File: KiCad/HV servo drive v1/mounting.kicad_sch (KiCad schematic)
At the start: 11 parts

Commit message: KiCad 8.0 update
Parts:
- renumbered H14 to H1, H8 to H10, H3 to H11, H13 to H2, H12 to H3, H10 to H4, H9 to H5, H4 to H8, H1 to H9

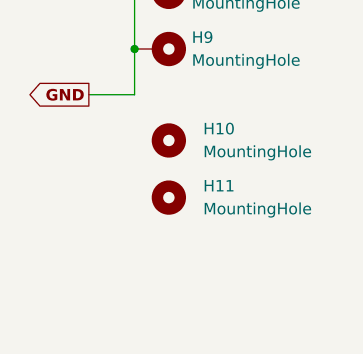
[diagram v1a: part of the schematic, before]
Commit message: start rev 2 changes
fix component references, fix rj45 and dc-dc converter footprints, add RLC filters on all power connectors, add more mounting holes
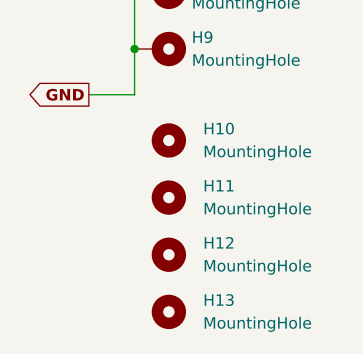
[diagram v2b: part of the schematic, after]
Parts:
- added H12, H13: MountingHole, footprints:MountingHole_3.2mm_M3_Pad_TopBottom_LargeIsolation, symbol Mechanical:MountingHole
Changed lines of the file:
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@@
+	)
+	(symbol
+		(lib_id "Mechanical:MountingHole")
+		(at 143.51 128.27 270)
+		(unit 1)
+		(exclude_from_sim no)
+		(in_bom yes)
+		(on_board yes)
+		(dnp no)
+		(fields_autoplaced yes)
+		(property "Reference" "H12"
+			(at 147.32 127 90)
+			(effects
+				(font
+					(size 1.27 1.27)
+				)
+				(justify left)
+			)
+		)
+		(property "Value" "MountingHole"
+			(at 147.32 129.54 90)
+			(effects
+				(font
+					(size 1.27 1.27)
+				)
+				(justify left)
+			)
+		)
+		(property "Footprint" "footprints:MountingHole_3.2mm_M3_Pad_TopBottom_LargeIsolation"
+			(at 143.51 128.27 0)
+			(effects
+				(font
+					(size 1.27 1.27)
+				)
+				(hide yes)
+			)
+		)
+		(property "Datasheet" "~"
+			(at 143.51 128.27 0)
+			(effects
+				(font
+					(size 1.27 1.27)
+				)
+				(hide yes)
+			)
+		)
+		(property "Description" ""
+			(at 143.51 128.27 0)
+			(effects
+				(font
+					(size 1.27 1.27)
+				)
+				(hide yes)
+			)
+		)
+		(instances
+			(project "HV servo drive v1"
+				(path "/00e1489f-e855-42b2-9b8a-dcc958a4feb6/5630d7aa-18e9-4c19-993b-fb61da4e222f"
+					(reference "H12")
+					(unit 1)
+				)
+			)
+		)
 	)
 	(symbol
@@
 					(unit 1)
 				)
+			)
+		)
+	)
+	(symbol
+		(lib_id "Mechanical:MountingHole")
+		(at 143.51 134.62 270)
+		(unit 1)
+		(exclude_from_sim no)
+		(in_bom yes)
+		(on_board yes)
+		(dnp no)
+		(fields_autoplaced yes)
+		(property "Reference" "H13"
+			(at 147.32 133.35 90)
+			(effects
+				(font
+					(size 1.27 1.27)
+				)
+				(justify left)
+			)
+		)
+		(property "Value" "MountingHole"
+			(at 147.32 135.89 90)
+			(effects
+				(font
+					(size 1.27 1.27)
+				)
+				(justify left)
+			)
+		)
+		(property "Footprint" "footprints:MountingHole_3.2mm_M3_Pad_TopBottom_LargeIsolation"
+			(at 143.51 134.62 0)
+			(effects
+				(font
+					(size 1.27 1.27)
+				)
+				(hide yes)
+			)
+		)
+		(property "Datasheet" "~"
+			(at 143.51 134.62 0)
+			(effects
+				(font
+					(size 1.27 1.27)
+				)
+				(hide yes)
+			)
+		)
+		(property "Description" ""
+			(at 143.51 134.62 0)
+			(effects
+				(font
+					(size 1.27 1.27)
+				)
+				(hide yes)
+			)
+		)
+		(instances
+			(project "HV servo drive v1"
+				(path "/00e1489f-e855-42b2-9b8a-dcc958a4feb6/5630d7aa-18e9-4c19-993b-fb61da4e222f"
+					(reference "H13")
+					(unit 1)
+				)

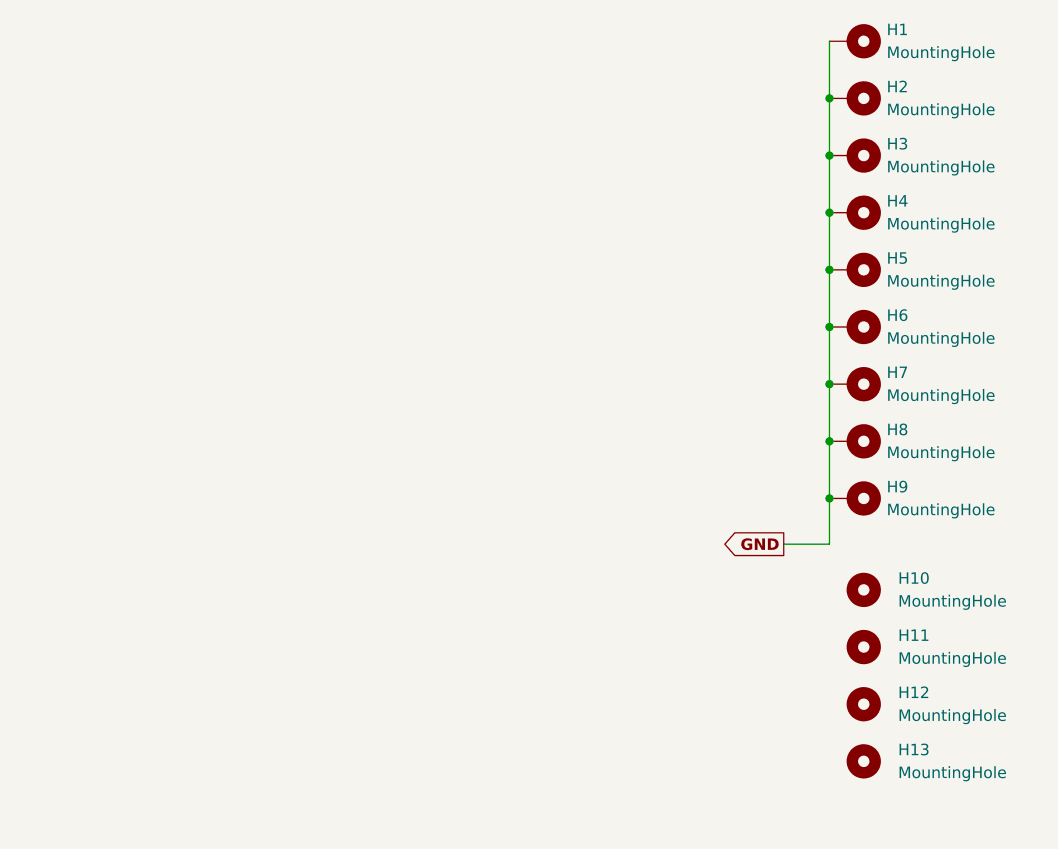
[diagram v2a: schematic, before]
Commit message: update to rev 2.1
basically the same version as in the FOC youtube video, with some minor issues fixed
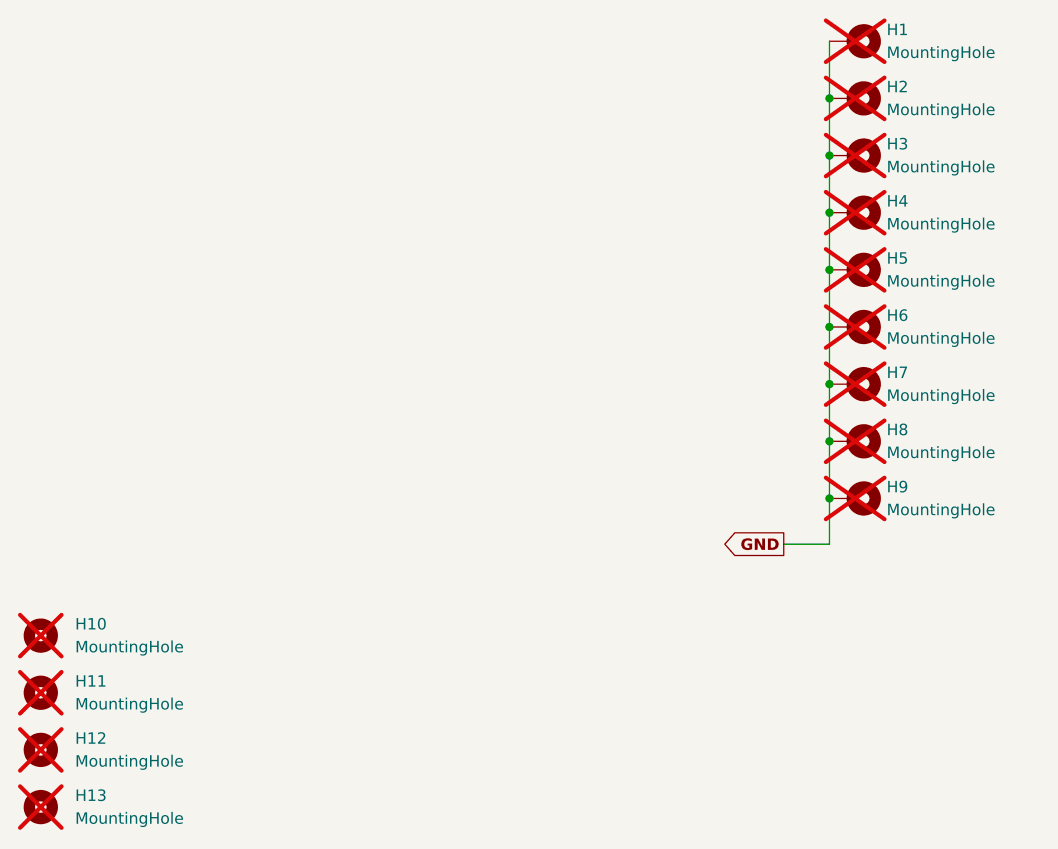
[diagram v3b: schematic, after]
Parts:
- H1, H10, H11, H12, H13, H2, H3, H4, H5, H6, H7, H8, H9: now not fitted
